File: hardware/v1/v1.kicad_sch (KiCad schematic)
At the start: 34 parts, among them J1 FPC 24P 0.5mm bottom contact, K1 GND, K2 DN_RX, K3 DN_TX, K4 DN_DET, K5 GND, P1 GND, P2 UP_TX, P3 UP_RX, P4 GND, P5 UP_DET, Q1 AO3400A, SW1 power, SW2 A: next, SW3 B: confirm, U1 Raspberry Pi Pico 2 (no heade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

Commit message: V1 schematic redrawn: the boost and power sections as circuits with wires, labelled blocks for the Pico and the connector, room between everything
Local net names on the drawn nets so the schematic's netlist still matches design.py and the
board. ERC clean. schematic.png added next to the board renders.
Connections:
- net N2 is gone; now on net GND: C3.2, D1.2 (A), D2.1 (K)
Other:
- note added: "Boost, as the panel spec's reference circuit (p. 28)."
- note added: "Buttons to ground. A next, B confirm."
- note added: "Cahoots badge V1: a board a Raspberry Pi Pico 2 solders onto. 54 x 86 mm, two layers. Labels with the same name are one net."
- note added: "Panel flex, GDEY0154D67 pin order (spec p. 7)."
- note added: "Pico 2. Module pin numbers outside, GPx inside."
- note added: "Pile contacts: face pads P1-P5 meet the spring contacts K1-K5 of the card above."
- note added: "Power: cell, switch, Schottky into VSYS."
- note added: "Rail capacitors, one per driven pin of the panel."
- note added: "design.py is the source; make_sch.py and make_pcb.py draw it; check.py confirms the schematic, the table and the board agree."
- note removed: "Boost: L1 47uH, Q1 switched by the panel's GDR pin, D3 to VGH (+), C3/D1/D2 pump VGL (-). R2 is the current sense."
- note removed: "Cahoots badge V1: a board a Raspberry Pi Pico 2 solders onto. 54 x 86 mm, two layers."
- note removed: "Connections are by net name: every pin carries a global label. design.py is the source; make_sch.py and make_pcb.py draw it."
- note removed: "Panel: GDEY0154D67 on a 24-pin 0.5 mm flex. Pinout and boost circuit from its specification (pp. 7, 28)."
- note removed: "Pile contacts: face pads P1-P5 (GND TX RX GND DET) meet the spring contacts K1-K5 of the card above."
- note removed: "Power: CR2032 > slide switch > Schottky > Pico VSYS. Buttons to ground on the chip's pull-ups."

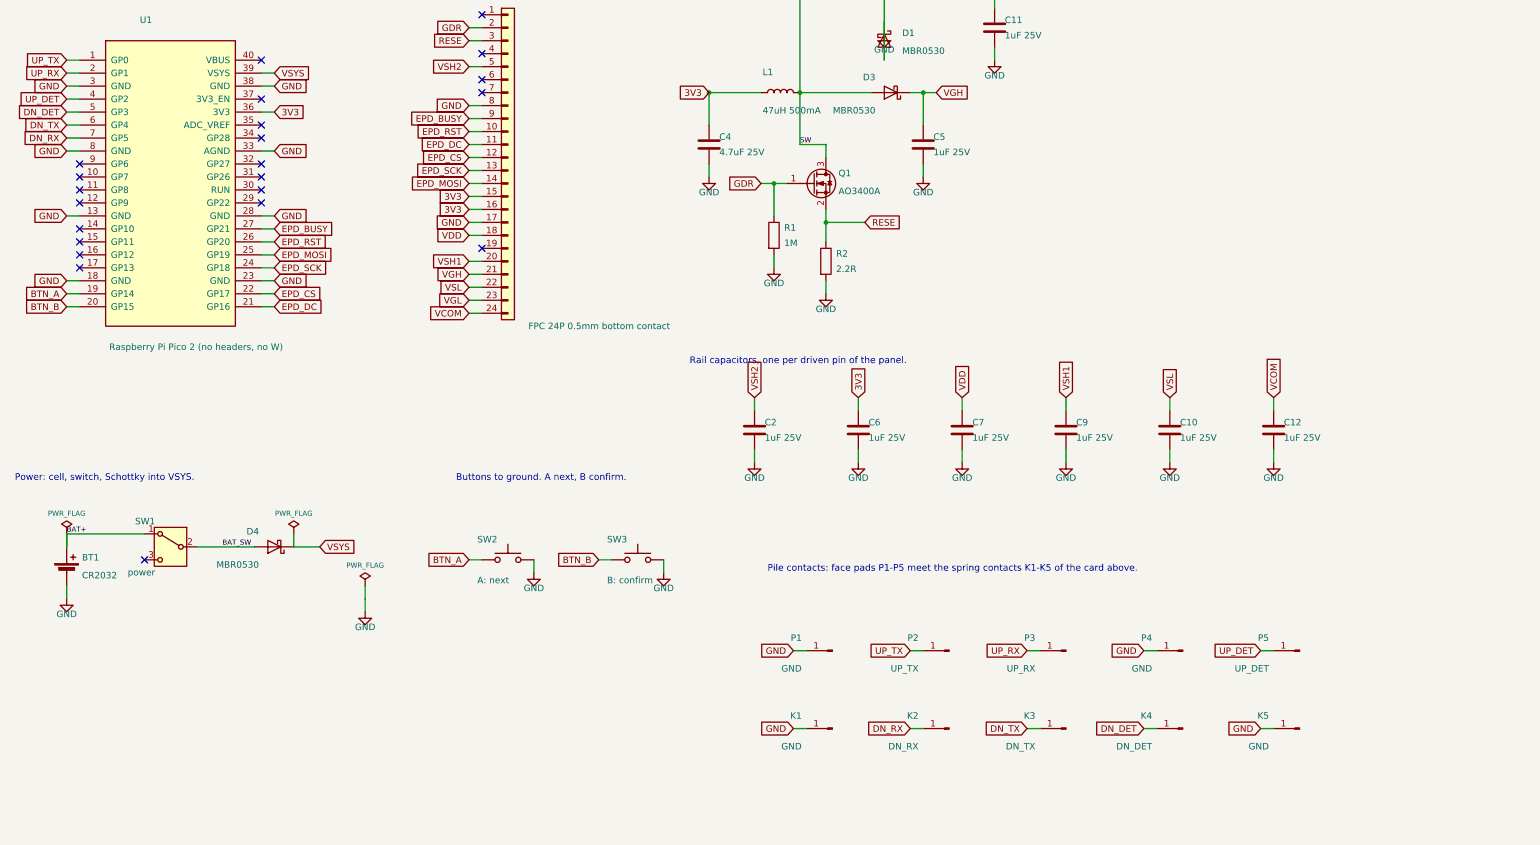
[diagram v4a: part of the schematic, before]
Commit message: V1: JST-SH UP and DN ports replace the pads and spring pins; cable openings in the case; switch and cell holder models; a sheet of each piece front and back
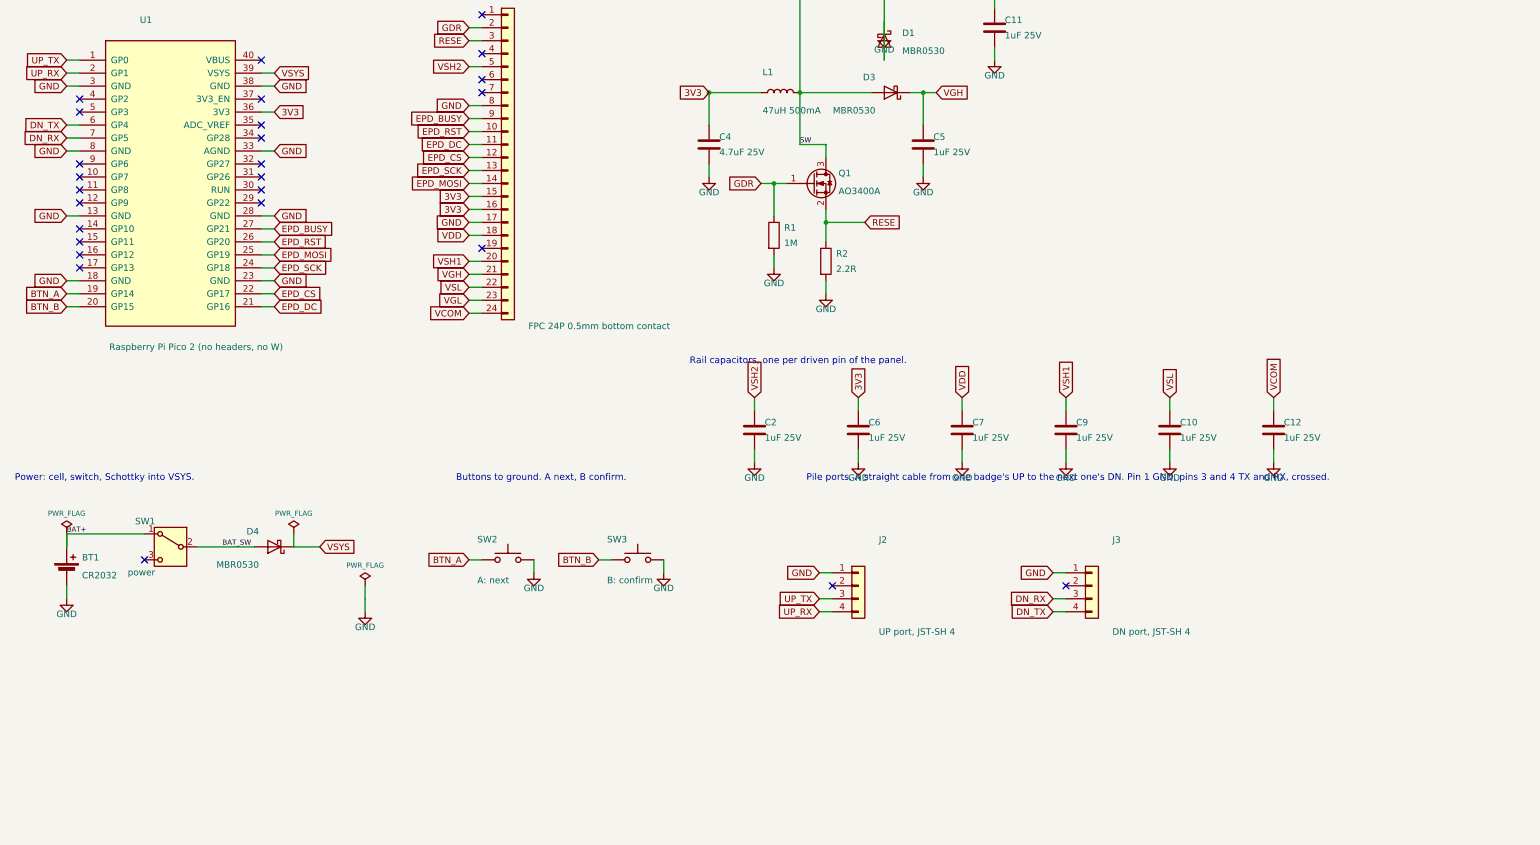
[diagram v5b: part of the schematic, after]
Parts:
- removed K1, K5: GND, cahoots:Pogo_SMD_D2.4mm, symbol Connector:Conn_01x01_Pin
- removed K2: DN_RX, cahoots:Pogo_SMD_D2.4mm, symbol Connector:Conn_01x01_Pin
- removed K3: DN_TX, cahoots:Pogo_SMD_D2.4mm, symbol Connector:Conn_01x01_Pin
- removed K4: DN_DET, cahoots:Pogo_SMD_D2.4mm, symbol Connector:Conn_01x01_Pin
- removed P1, P4: GND, cahoots:Pad_D3.5mm, symbol Connector:Conn_01x01_Pin
- removed P2: UP_TX, cahoots:Pad_D3.5mm, symbol Connector:Conn_01x01_Pin
- removed P3: UP_RX, cahoots:Pad_D3.5mm, symbol Connector:Conn_01x01_Pin
- removed P5: UP_DET, cahoots:Pad_D3.5mm, symbol Connector:Conn_01x01_Pin
- added J2: UP port, JST-SH 4, Connector_JST:JST_SH_SM04B-SRSS-TB_1x04-1MP_P1.00mm_Horizontal, symbol Connector_Generic:Conn_01x04
- added J3: DN port, JST-SH 4, Connector_JST:JST_SH_SM04B-SRSS-TB_1x04-1MP_P1.00mm_Horizontal, symbol Connector_Generic:Conn_01x04
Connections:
- net DN_RX: now also J3.3 (Pin_3)
- net DN_TX: now also J3.4 (Pin_4)
- net GND: now also J2.1 (Pin_1), J3.1 (Pin_1)
- net UP_RX: now also J2.4 (Pin_4)
- net UP_TX: now also J2.3 (Pin_3)
- net DN_DET: no longer names the net of U1.5 (GP3)
- net UP_DET: no longer names the net of U1.4 (GP2)
- no-connect marks 22 -> 26
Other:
- note added: "Pile ports. A straight cable from one badge's UP to the next one's DN. Pin 1 GND, pins 3 and 4 TX and RX, crossed."
- note removed: "Pile contacts: face pads P1-P5 meet the spring contacts K1-K5 of the card above."

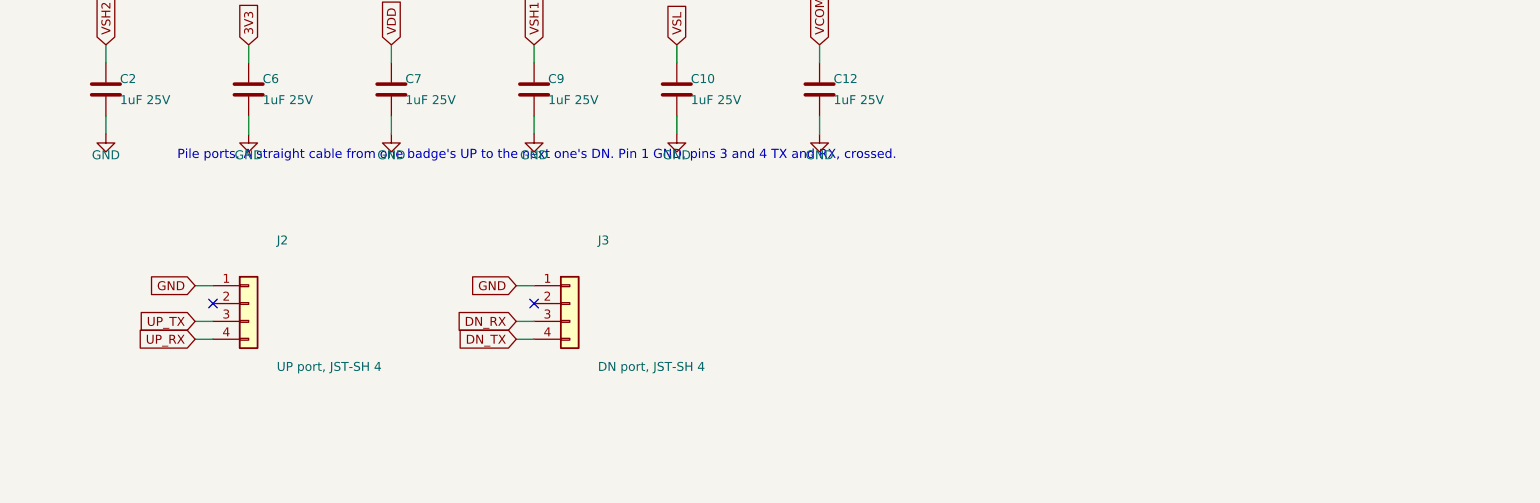
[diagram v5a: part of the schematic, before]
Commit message: V1: magnetic pogo pair at both ends (Adafruit 5359), faces flush with the case; JST sockets moved beside it; lanyard slot gone; round models as face sets so magnets, cell and pins render; end view on the assembly sheet
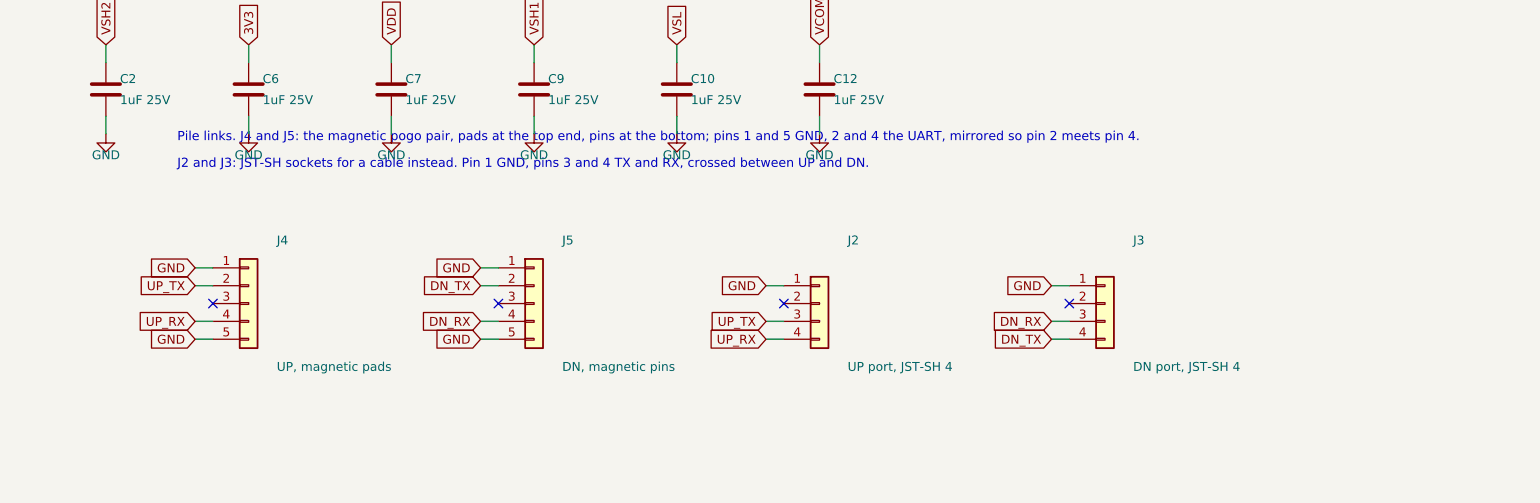
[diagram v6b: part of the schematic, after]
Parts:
- added J4: UP, magnetic pads, cahoots:Pogo_MG05254_RA_1x05, symbol Connector_Generic:Conn_01x05
- added J5: DN, magnetic pins, cahoots:Pogo_MG05254_RA_1x05, symbol Connector_Generic:Conn_01x05
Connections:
- net DN_RX: now also J5.4 (Pin_4)
- net DN_TX: now also J5.2 (Pin_2)
- net GND: now also J4.1 (Pin_1), J4.5 (Pin_5), J5.1 (Pin_1), J5.5 (Pin_5)
- net UP_RX: now also J4.4 (Pin_4)
- net UP_TX: now also J4.2 (Pin_2)
- no-connect marks 26 -> 28
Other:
- note added: "J2 and J3: JST-SH sockets for a cable instead. Pin 1 GND, pins 3 and 4 TX and RX, crossed between UP and DN."
- note added: "Pile links. J4 and J5: the magnetic pogo pair, pads at the top end, pins at the bottom; pins 1 and 5 GND, 2 and 4 the UART, mirrored so pin 2 meets pin 4."
- note removed: "Pile ports. A straight cable from one badge's UP to the next one's DN. Pin 1 GND, pins 3 and 4 TX and RX, crossed."

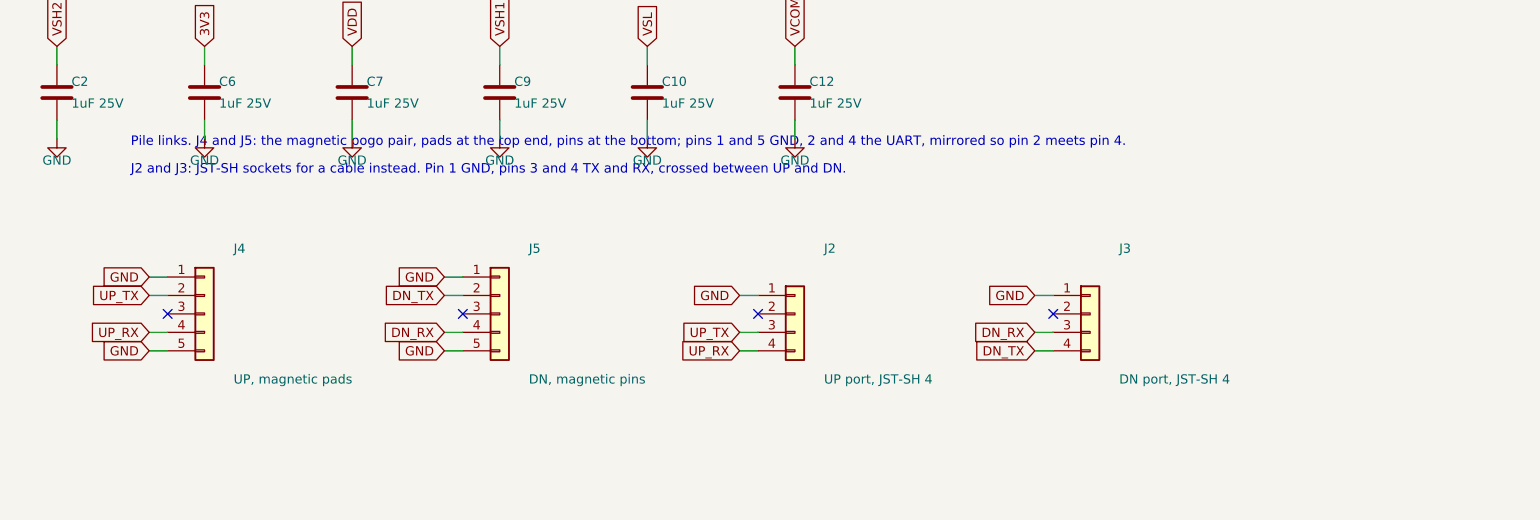
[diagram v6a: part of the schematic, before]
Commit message: V1: stack face to face. Straight magnetic pogo pair (Adafruit 5413): pin half on the board, pins up through the lid; pad half flush in the tray floor on a pigtail to DN. Lid cavity 2.2, badge 13.4 mm; skirt down to snaps below the board; stacked view on the sheet
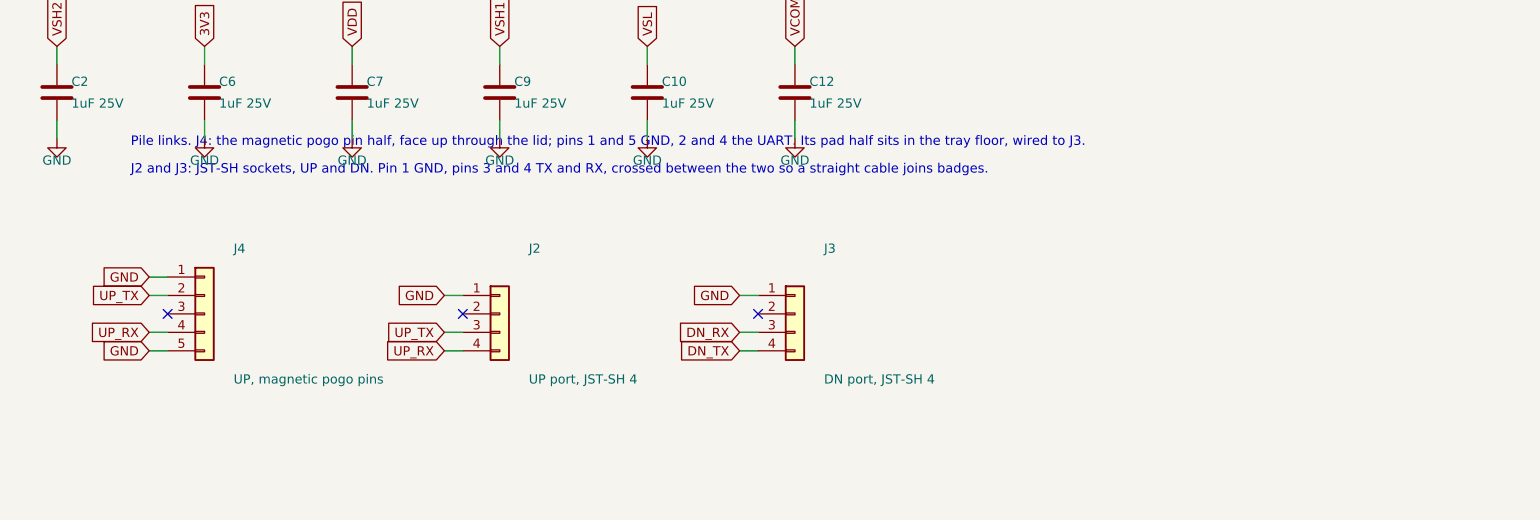
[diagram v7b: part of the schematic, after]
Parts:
- removed J5: DN, magnetic pins, cahoots:Pogo_MG05254_RA_1x05, symbol Connector_Generic:Conn_01x05
- J4: value UP, magnetic pads -> UP, magnetic pogo pins; footprint cahoots:Pogo_MG05254_RA_1x05 -> cahoots:Pogo_MG005_1x05; LCSC Adafruit 5359 pad half, MG05254-R-RA-1N1S -> Adafruit 5413 pair, pin half
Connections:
- no-connect marks 28 -> 27
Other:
- note added: "J2 and J3: JST-SH sockets, UP and DN. Pin 1 GND, pins 3 and 4 TX and RX, crossed between the two so a straight cable joins badges."
- note added: "Pile links. J4: the magnetic pogo pin half, face up through the lid; pins 1 and 5 GND, 2 and 4 the UART. Its pad half sits in the tray floor, wired to J3."
- note removed: "J2 and J3: JST-SH sockets for a cable instead. Pin 1 GND, pins 3 and 4 TX and RX, crossed between UP and DN."
- note removed: "Pile links. J4 and J5: the magnetic pogo pair, pads at the top end, pins at the bottom; pins 1 and 5 GND, 2 and 4 the UART, mirrored so pin 2 meets pin 4."
